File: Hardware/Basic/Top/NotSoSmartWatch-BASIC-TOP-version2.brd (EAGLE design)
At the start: 38 x 38 mm, 50 parts, among them SW3 SWITCH.MOM, SW4 SWITCH.MOM, U1 NRF52832_MODULE_MDBT42

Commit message: almost done with Take 007
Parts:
- C17: device LinnesLab-Passives:C0402 -> LinnesLab-Passives:C0603
- moved R18 16.7 mm to (20.9, 11.6)
- moved R17 11.7 mm to (20.9, 9.78)
- moved C17 10.9 mm to (29.1, 14.5), turned to 180 degrees
- moved R1 10.8 mm to (1.60, 29.9), turned to 270 degrees
- moved R2 8.10 mm to (3.28, 29.9), turned to 270 degrees
- moved C14 3.20 mm to (2.84, 12.2), turned to 180 degrees
- moved C2 2.91 mm to (17.2, 31.6), turned to 0 degrees
- moved L1 2.66 mm to (17.2, 28.2), turned to 0 degrees
- moved C1 2.60 mm to (16.8, 29.8), turned to 180 degrees
- moved JP1 1.54 mm to (2.92, 3.07)
- moved FTDI 1.44 mm to (6.40, 7.77)
- moved J1 1.27 mm to (5.08, 33.0)
- moved R16 1.02 mm to (12.6, 10.7)
- moved LED3 0.95 mm to (16.2, 9.19)
- moved R14 0.93 mm to (12.4, 9.17)
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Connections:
- net !CTS renamed CTS
- removed net !DTR: FTDI.1
- removed net A4/VBATT: R8.1, R9.2, U1.5
- removed net A6/TIA: U1.7
- removed net A7/PPG: U1.8
- removed net D29/LED.CTRL: U1.6
- removed net N$21: J1.5
- removed net N$22: J1.4
- removed net N$27: J1.3
- removed net N$28: J1.2
- removed net N$29: J1.1
- new net A4/PPG: J1.7, U1.5
- new net A5/TIA: J1.6, U1.6
- new net A7/BATT: R8.1, R9.2, U1.8
- new net D30/LED.CTRL: J1.5, U1.7
- net 3.3V: now also J1.4; no longer J1.7
- net DTR: now also FTDI.1
- net GND: now also J1.3; no longer J1.6
- net SCL: now also J1.2
- net SDA: now also J1.1
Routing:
- net DTR: track 0.00 -> 39.2 mm, vias 0 -> 2
- net SDA: track 0.00 -> 23.8 mm, vias 0 -> 1
- net SCL: track 0.00 -> 22.4 mm, vias 0 -> 1
- net A7/BATT: track 0.00 -> 19.8 mm, vias 0 -> 2
- net D16/CS.OLED: track 0.00 -> 19.4 mm, vias 0 -> 2
- net RXD.NRF: track 0.00 -> 18.7 mm, vias 0 -> 2
- net SCK: track 0.00 -> 18.4 mm, vias 0 -> 2
- net MOSI: track 0.00 -> 17.3 mm, vias 0 -> 2
- net TXD.NRF: track 0.00 -> 16.3 mm, vias 0 -> 2
- net D30/LED.CTRL: track 0.00 -> 15.7 mm, vias 0 -> 1
- net A5/TIA: track 0.00 -> 14.2 mm, vias 0 -> 1
- net GND: track 64.8 -> 50.7 mm, vias 19 -> 26
- net D4/DC.OLED: track 0.00 -> 13.0 mm, vias 0 -> 2
- net A4/PPG: track 0.00 -> 12.8 mm, vias 0 -> 1
- net D3/RESET.OLED: track 0.00 -> 12.5 mm, vias 0 -> 2
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
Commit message: updated through Take 007 - not sure if I have an isolated polygon
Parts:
- added C5, C7: 4.7u, LinnesLab-Passives:C0603
- added C8, C9: 1u, LinnesLab-Passives:C0603
- added CHRG: MCP73831, LinnesLab-Power:SOT23-5
- added LDO1: MIC5504, LinnesLab-Power:SOT23-5
- added R3, R7: 100k, LinnesLab-Passives:R0603
- added R6: (no value), LinnesLab-Passives:R0603
- moved R1 3.91 mm to (1.73, 33.8), turned to 90 degrees
- moved R2 3.86 mm to (3.25, 33.8), turned to 90 degrees
- moved C18 1.11 mm to (8.10, 22.7)
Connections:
- new net N$16: CHRG.5, R6.2
- net 3.3V: now also C9.1, LDO1.5, R7.2
- net D27/CHRG.STAT: now also CHRG.1, R3.1
- net GND: now also C5.2, C7.1, C8.1, C9.2, CHRG.2, LDO1.2, R6.1, R7.1
- net VIN: now also C7.2, C8.2, CHRG.4, LDO1.1, LDO1.3, R3.2
- net VLIPO: now also C5.1, CHRG.3
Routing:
- net VIN: track 4.65 -> 45.1 mm, vias 0 -> 1
- net D27/CHRG.STAT: track 0.00 -> 27.2 mm, vias 0 -> 4
- net GND: track 50.7 -> 67.5 mm, vias 26 -> 31
- net VLIPO: track 18.6 -> 32.3 mm, vias 0 -> 1
- net 3.3V: track 0.00 -> 7.84 mm
- net A7/BATT: track 19.8 -> 22.1 mm
- net N$16: track 0.00 -> 1.69 mm
- net D30/LED.CTRL: track 15.7 -> 14.7 mm
- net SDA: track 23.8 -> 24.3 mm

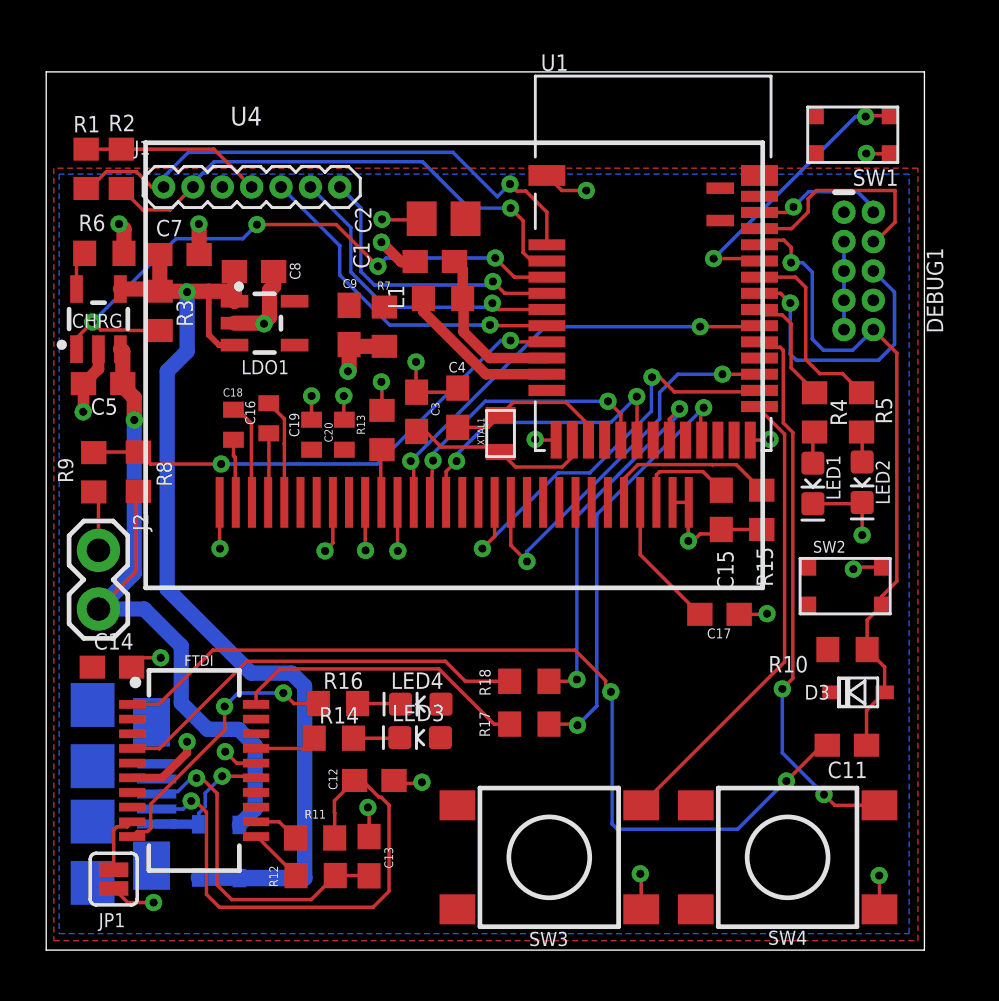
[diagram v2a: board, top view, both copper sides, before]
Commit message: updated through Take 008 - there's some airwires I don't understand, might be polygon related
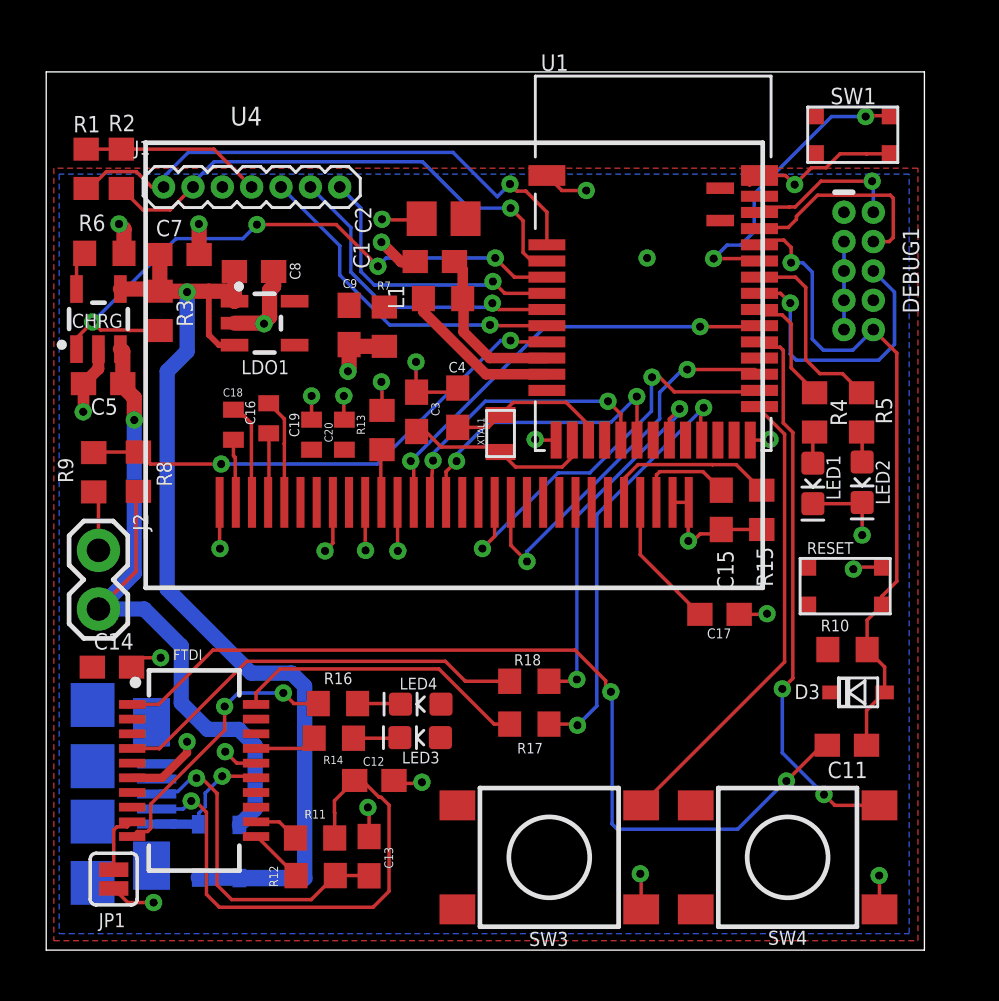
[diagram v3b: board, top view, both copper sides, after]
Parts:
- R6: value (none) -> 5k
- renumbered SW2 to RESET
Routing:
- net GND: track 67.5 -> 73.5 mm, vias 31 -> 32
- net DFU: track 12.2 -> 13.2 mm
- net SWDIO: track 5.87 -> 6.80 mm

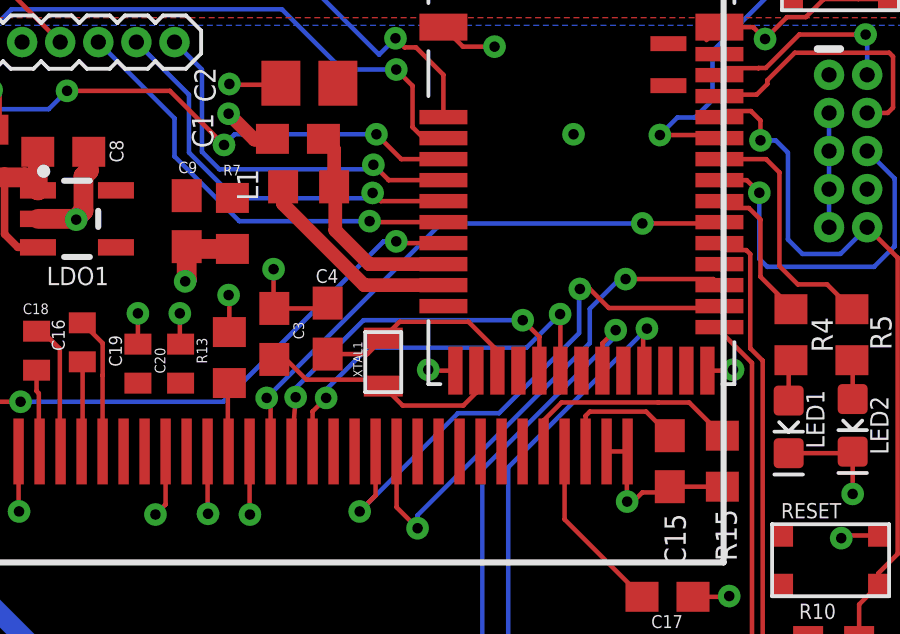
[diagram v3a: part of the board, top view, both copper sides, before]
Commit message: fixed isolated polygon - should be good now
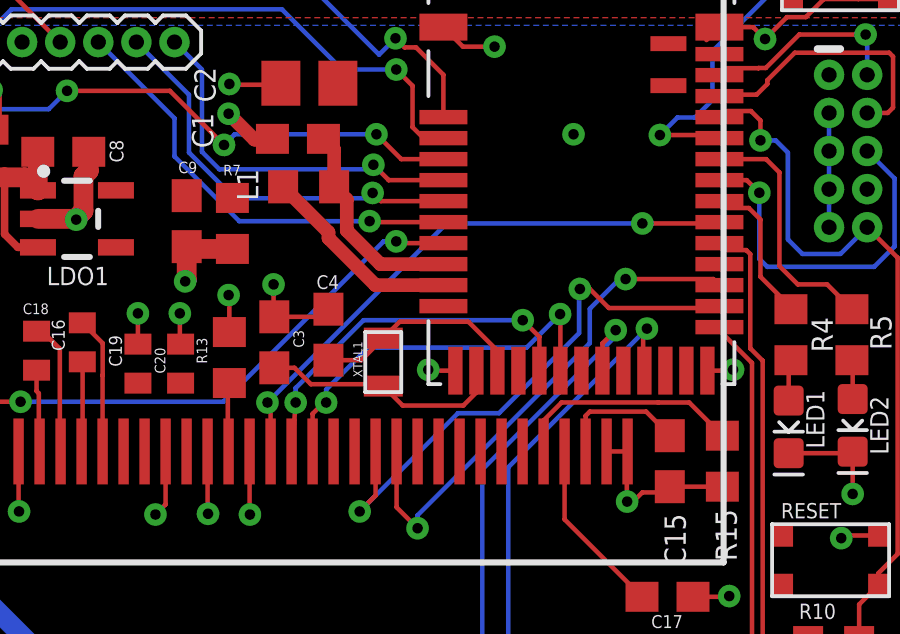
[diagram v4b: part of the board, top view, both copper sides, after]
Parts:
- moved C3 0.28 mm to (16.0, 23.0)
- moved C4 0.20 mm to (17.8, 23.3)
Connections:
- net GND: no longer SW3.B2, SW4.B2
